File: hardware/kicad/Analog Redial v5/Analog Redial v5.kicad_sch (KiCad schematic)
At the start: 64 parts, among them J1 Barrel_Jack_PTH_Slot, J3 PINHD_1x2_Male, J4 PINHD_1x2_Male, J5 PINHD_2x4_Male, J7 PINHD_1x3_Male, J8 RJ12, J9 RJ12, U1 ESP32-C6-DevKitC-1, U2 ES8388, U3 AG1171, U4 AG1171

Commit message: Rename KiCad projects to Analog Redial v2/v3/v4/v5
Rotary_phone_SMD2 -> "Analog Redial v2", Old/Rotary_phone_SMD3 ->
"Old/Analog Redial v3", Rotary_phone_SMD4 -> "Analog Redial v4", and
"Analog Redial 5" -> "Analog Redial v5": directories, project files, and the
project-name references inside them (schematic annotation instances, the
PCB's sheet-file fields), checked by exporting each netlist -- every part is
still annotated. Silkscreen text and the SMD2 Gerber outputs keep their
names. Doc and code references updated (link targets URL-encoded); two
already-broken SMD2 BOM CSV links fixed on the way.

Firmware board-type names (CONFIG_BOARD_TYPE_SMD2/SMD4/SMD5) unchanged.

Co-Authored-By: Claude Opus 5.5 <noreply@anthropic.com>
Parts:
- added C22, C23, C24, C25, C26: 1uF, Capacitor_SMD:C_0402_1005Metric, symbol PCM_SparkFun-Capacitor:C_Small
- added J2: PINHD_1x8_Male, Connector_PinHeader_2.54mm:PinHeader_1x08_P2.54mm_Vertical, symbol PCM_SL_Pin_Headers:PINHD_1x8_Male
- added JP2, JP3: (no value), PCM_SparkFun-Jumper:Jumper_3_NC-1_Trace_NoSilk, symbol Jumper:SolderJumper_3_Bridged12
- added R16: 1k, Resistor_SMD:R_0402_1005Metric, symbol PCM_SparkFun-Resistor:R
- added R17: 100k, Resistor_SMD:R_0402_1005Metric, symbol PCM_SparkFun-Resistor:R
- added U5: XC6206P332MR, Package_TO_SOT_SMD:SOT-23-3, symbol Regulator_Linear:XC6206PxxxMR
- C10, C11: value 100uF -> 47uF; footprint Capacitor_SMD:C_1206_3216Metric -> Capacitor_THT:C_Disc_D4.7mm_W2.5mm_P5.00mm
- R12, R14: value 15k -> 100k
- U1: footprint PCM_Espressif:ESP32-C6-DevKitC-1 -> Custom:ESP32-C6-DevKitC-dual
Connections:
- net +5V: now also C26.1, U5.3 (VI)
- net GND: now also C24.1, C25.2, C26.2, J2.8, R17.1, U5.1 (GND)
- net I2S_MCLK: now also JP3.2 (C); no longer U1.12 (GPIO2)
- net SD_CD: now also JP2.2 (C); no longer U1.13 (GPIO3)
- net Line0Vin: now reaches C12.2, U4.9 (Vin)
- net Line0Vin: now also R16.1
- net at U1.30 (GPIO17/U0RXD): now also J2.2; no longer J4.1
- net at U1.31 (GPIO16/U0TXD): now also J2.3; no longer J3.1
- net GPIO12: now reaches U1.19 (GPIO12/USB_D-)
- net GPIO12: now also J4.1, JP3.3 (B)
- net GPIO13: now reaches U1.20 (GPIO13/USB_D+)
- net GPIO13: now also J3.1, JP2.3 (B)
- net MFB: now reaches U1.29 (GPIO15/JTAG)
- net MFB: now also J2.4, R17.2
- net Line0Vout: now reaches C13.2, U4.10 (Vout)
- net Line0Vout: now also C22.1
- new net: C24.2, J2.6
- new net: C23.1, R16.2
- new net: C23.2, J2.7
- new net: JP3.1 (A), U1.12 (GPIO2)
- new net: JP2.1 (A), U1.13 (GPIO3)
- new net: C22.2, J2.5
- new net +3.3V_BM: C25.1, J2.1, U5.2 (VO)
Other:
- note added: "Bluetooth BM64 header"
- note added: "CF Card"
- note added: "Changes for SMD4: capacitor silkscreen needs to show capacitance value and line silkscreen note to add jumpbers for 2nd AG1171 silkscreen note to only use uSD OR SLIC #2 increase capacitor clearance and update footprint clearance to AG1171 board New esp32-c6 wide version option. (big change) add cuttable jumpers to select correct pinout for wide/cheap esp32-c6 change SHK voltage divider so it's c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"
- note added: "Line 0: Left"
- note added: "Line 1: Right"
- note added: "UART to bluetooth board"
- note added: "pin 5&6 matching cap mic inputs"
- note removed: "Fixes needed for SMD4: capacitor silkscreen needs to show capacitance value larger holes for esp32 silkscreen note to add jumpbers for 2nd AG1171 silkscreen note to only use uSD OR SLIC #2 increase capacitor clearance and update footprint clearance to AG1171 board"
- note removed: "Line 1: Left"
- note removed: "Line 2: Right"
- note removed: "NC D+"
- note removed: "NC D-"
- note removed: "NC Jtag"
- note removed: "Use as UART header or 2x GPIO"
- moved on the sheet: C1, Card1, H1, H2, H3, H4, R1, R2

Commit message: v5 schematic: fix note wording (changes from SMD4)
Co-Authored-By: Claude Sonnet 5.5 <noreply@anthropic.com>
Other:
- note added: "Changes from SMD4: capacitor silkscreen needs to show capacitance value and line silkscreen note to add jumpbers for 2nd AG1171 silkscreen note to only use uSD OR SLIC #2 increase capacitor clearance and update footprint clearance to AG1171 board New esp32-c6 wide version option. (big change) add cuttable jumpers to select correct pinout for wide/cheap esp32-c6 change SHK voltage divider so it's 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"
- note removed: "Changes for SMD4: capacitor silkscreen needs to show capacitance value and line silkscreen note to add jumpbers for 2nd AG1171 silkscreen note to only use uSD OR SLIC #2 increase capacitor clearance and update footprint clearance to AG1171 board New esp32-c6 wide version option. (big change) add cuttable jumpers to select correct pinout for wide/cheap esp32-c6 change SHK voltage divider so it's c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"
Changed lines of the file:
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@@
 		)
 	)
-	(text "Changes for SMD4:\ncapacitor silkscreen needs to show capacitance value and line\nsilkscreen note to add jumpbers for 2nd AG1171\nsilkscreen note to only use uSD OR SLIC #2\nincrease capacitor clearance and update footprint clearance to AG1171 board\nNew esp32-c6 wide version option. (big change)\n	add cuttable jumpers to select correct pinout for wide/cheap esp32-c6\n\nchange SHK voltage divider so it's closer to 3.3V output (currently it's measuring 1.8V)\n	by swapping the 15k for 100k to gnd.\n\nadd 8-pin header for bluetooth module.\nadd pull-down 100k to MFB line, connected to GPIO15\nAdd 3.3V regulator for optional bluetooth module\n\n"
+	(text "Changes from SMD4:\ncapacitor silkscreen needs to show capacitance value and line\nsilkscreen note to add jumpbers for 2nd AG1171\nsilkscreen note to only use uSD OR SLIC #2\nincrease capacitor clearance and update footprint clearance to AG1171 board\nNew esp32-c6 wide version option. (big change)\n	add cuttable jumpers to select correct pinout for wide/cheap esp32-c6\n\nchange SHK voltage divider so it's closer to 3.3V output (currently it's measuring 1.8V)\n	by swapping the 15k for 100k to gnd.\n\nadd 8-pin header for bluetooth module.\nadd pull-down 100k to MFB line, connected to GPIO15\nAdd 3.3V regulator for optional bluetooth module\n\n"
 		(exclude_from_sim no)
 		(at 198.628 61.214 0)

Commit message: KiCad v5: edits as of 2026-10-19
Co-Authored-By: Claude Opus 5.5 <noreply@anthropic.com>
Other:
- note added: "Issues with SMD5: Major flaw in dual ESP32 footprint: the 2nd 5V pad was tied to ground. Fix: don't populate that pin (18)"
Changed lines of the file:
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@@
+		)
+	)
+	(text "Issues with SMD5:\nMajor flaw in dual ESP32 footprint:  the 2nd 5V pad was tied to ground. \nFix:  don't populate that pin (18)"
+		(exclude_from_sim no)
+		(at 199.39 60.706 0)
+		(effects
+			(font
+				(size 1.27 1.27)
+			)
+			(justify left)
 		)
 	)
@@
 	(text "Changes from SMD4:\ncapacitor silkscreen needs to show capacitance value and line\nsilkscreen note to add jumpbers for 2nd AG1171\nsilkscreen note to only use uSD OR SLIC #2\nincrease capacitor clearance and update footprint clearance to AG1171 board\nNew esp32-c6 wide version option. (big change)\n	add cuttable jumpers to select correct pinout for wide/cheap esp32-c6\n\nchange SHK voltage divider so it's closer to 3.3V output (currently it's measuring 1.8V)\n	by swapping the 15k for 100k to gnd.\n\nadd 8-pin header for bluetooth module.\nadd pull-down 100k to MFB line, connected to GPIO15\nAdd 3.3V regulator for optional bluetooth module\n\n"
 		(exclude_from_sim no)
-		(at 198.628 61.214 0)
+		(at 199.136 38.1 0)
 		(effects
 			(font

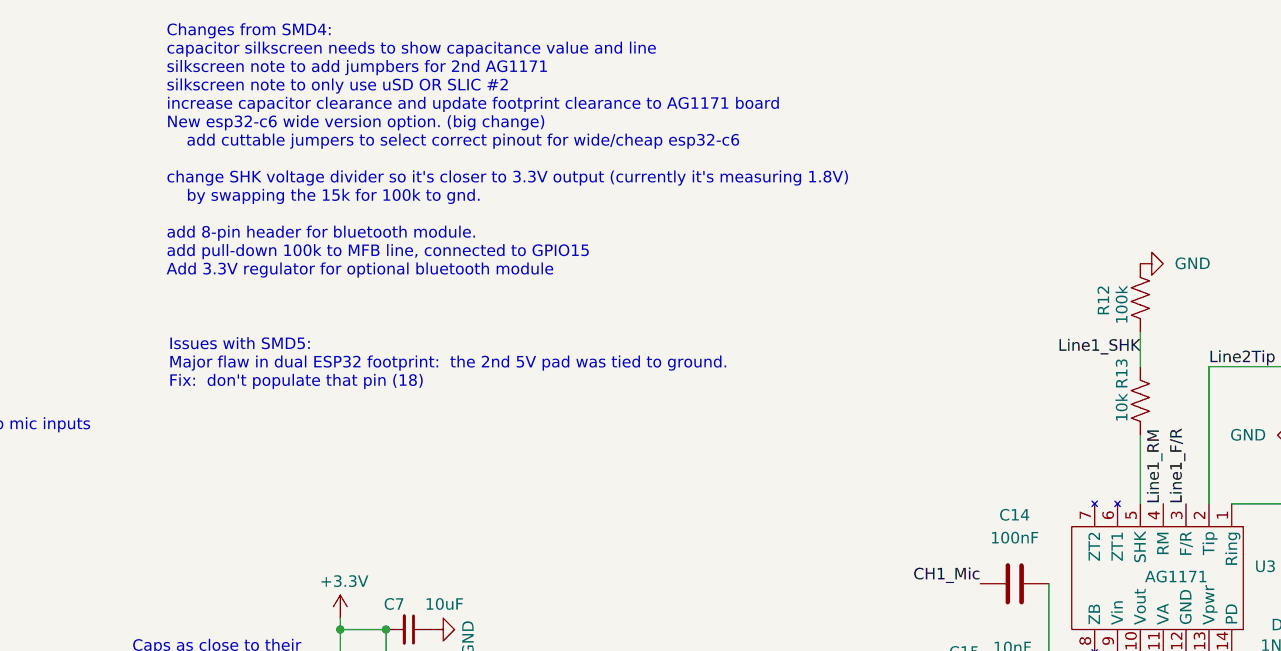
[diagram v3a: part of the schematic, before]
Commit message: v5 back to the as-fabbed files; v5.1 = v5 with the clone 5V-pin fix; track every board's JLCPCB/PCBWay exports. Docs: expansion header (J2) with its pinout, payphone section. Echo test: quiet the line before measuring (dial tone hid the echo). Wi-Fi power-save allowed with board-to-board numbers
Co-Authored-By: Claude Opus 5.5 <noreply@anthropic.com>
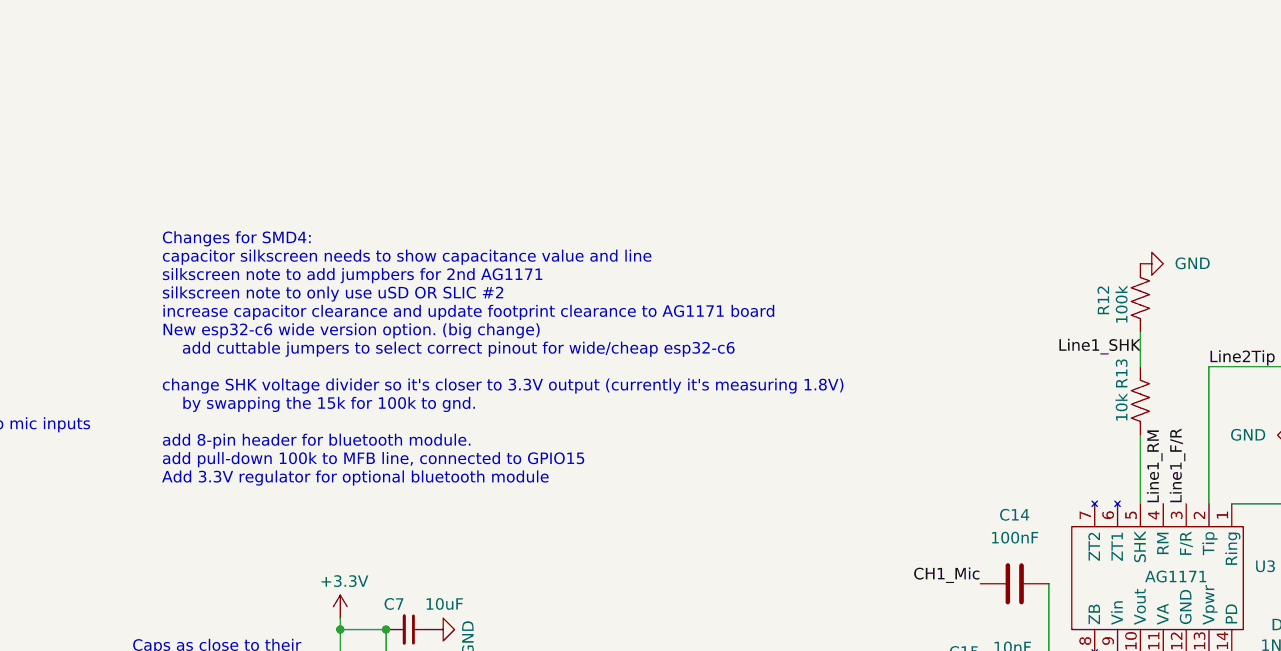
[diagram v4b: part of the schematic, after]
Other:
- note added: "Changes for SMD4: capacitor silkscreen needs to show capacitance value and line silkscreen note to add jumpbers for 2nd AG1171 silkscreen note to only use uSD OR SLIC #2 increase capacitor clearance and update footprint clearance to AG1171 board New esp32-c6 wide version option. (big change) add cuttable jumpers to select correct pinout for wide/cheap esp32-c6 change SHK voltage divider so it's c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"
- note removed: "Changes from SMD4: capacitor silkscreen needs to show capacitance value and line silkscreen note to add jumpbers for 2nd AG1171 silkscreen note to only use uSD OR SLIC #2 increase capacitor clearance and update footprint clearance to AG1171 board New esp32-c6 wide version option. (big change) add cuttable jumpers to select correct pinout for wide/cheap esp32-c6 change SHK voltage divider so it's 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"
- note removed: "Issues with SMD5: Major flaw in dual ESP32 footprint: the 2nd 5V pad was tied to ground. Fix: don't populate that pin (18)"
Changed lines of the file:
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@@
-		)
-	)
-	(text "Issues with SMD5:\nMajor flaw in dual ESP32 footprint:  the 2nd 5V pad was tied to ground. \nFix:  don't populate that pin (18)"
-		(exclude_from_sim no)
-		(at 199.39 60.706 0)
-		(effects
-			(font
-				(size 1.27 1.27)
-			)
-			(justify left)
 		)
 	)
@@
 		)
 	)
-	(text "Changes from SMD4:\ncapacitor silkscreen needs to show capacitance value and line\nsilkscreen note to add jumpbers for 2nd AG1171\nsilkscreen note to only use uSD OR SLIC #2\nincrease capacitor clearance and update footprint clearance to AG1171 board\nNew esp32-c6 wide version option. (big change)\n	add cuttable jumpers to select correct pinout for wide/cheap esp32-c6\n\nchange SHK voltage divider so it's closer to 3.3V output (currently it's measuring 1.8V)\n	by swapping the 15k for 100k to gnd.\n\nadd 8-pin header for bluetooth module.\nadd pull-down 100k to MFB line, connected to GPIO15\nAdd 3.3V regulator for optional bluetooth module\n\n"
+	(text "Changes for SMD4:\ncapacitor silkscreen needs to show capacitance value and line\nsilkscreen note to add jumpbers for 2nd AG1171\nsilkscreen note to only use uSD OR SLIC #2\nincrease capacitor clearance and update footprint clearance to AG1171 board\nNew esp32-c6 wide version option. (big change)\n	add cuttable jumpers to select correct pinout for wide/cheap esp32-c6\n\nchange SHK voltage divider so it's closer to 3.3V output (currently it's measuring 1.8V)\n	by swapping the 15k for 100k to gnd.\n\nadd 8-pin header for bluetooth module.\nadd pull-down 100k to MFB line, connected to GPIO15\nAdd 3.3V regulator for optional bluetooth module\n\n"
 		(exclude_from_sim no)
-		(at 199.136 38.1 0)
+		(at 198.628 61.214 0)
 		(effects
 			(font
